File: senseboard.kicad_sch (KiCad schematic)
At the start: 81 parts, among them J1 USB_C_Receptacle_USB2.0_16P, J2 Screw_Terminal_01x02, J3 DM3AT-SF-PEJM5, J4 Conn_01x04, J5 Conn_01x08, U1 USBLC6-2SC6, U10 EMIF06-MSD02N16, U11 BME690, U2 TPS62840DLCR, U3 TPS62840DLCR, U4 SCD41-D-R2, U5 SGP41-D-R4, U6 SGP41-D-R4, U7 SHT4x, U8 STM32L4Q5CGUx, U9 RFM95W-915S2, Y1 Crystal_GND3

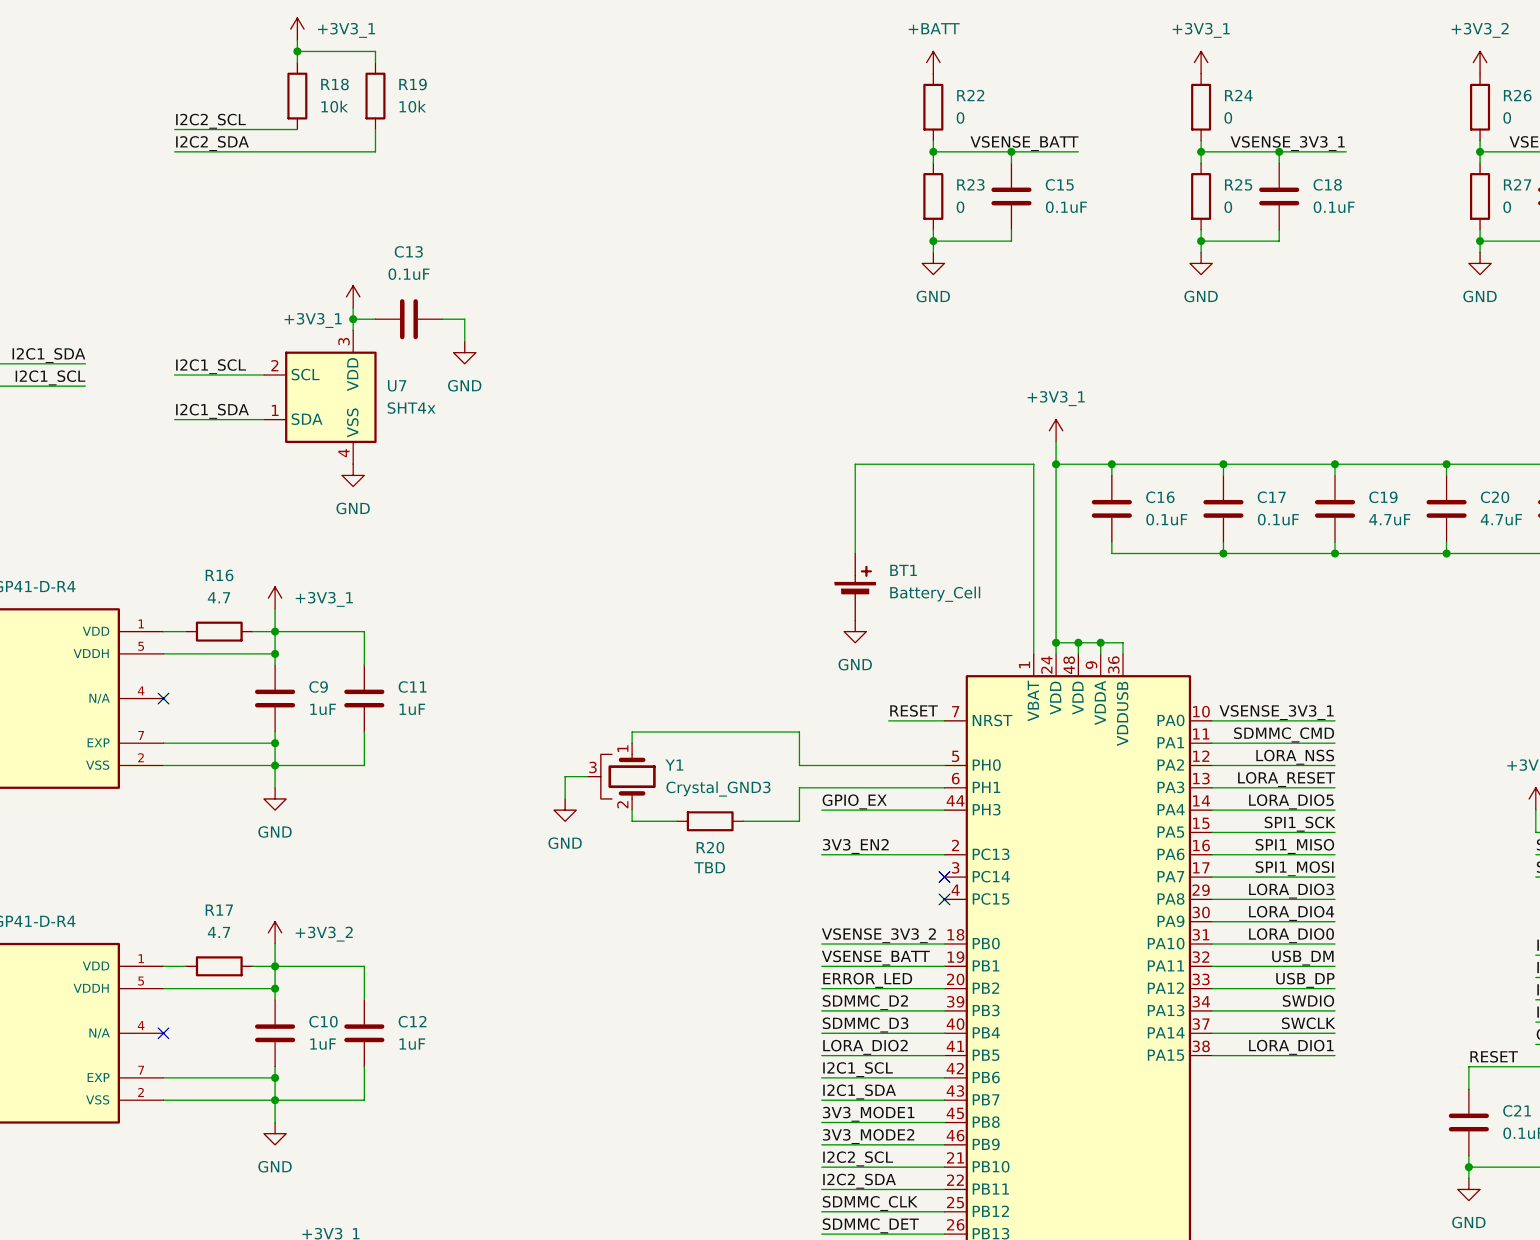
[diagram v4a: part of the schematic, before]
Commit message: connected n/a on sgp41 to gnd
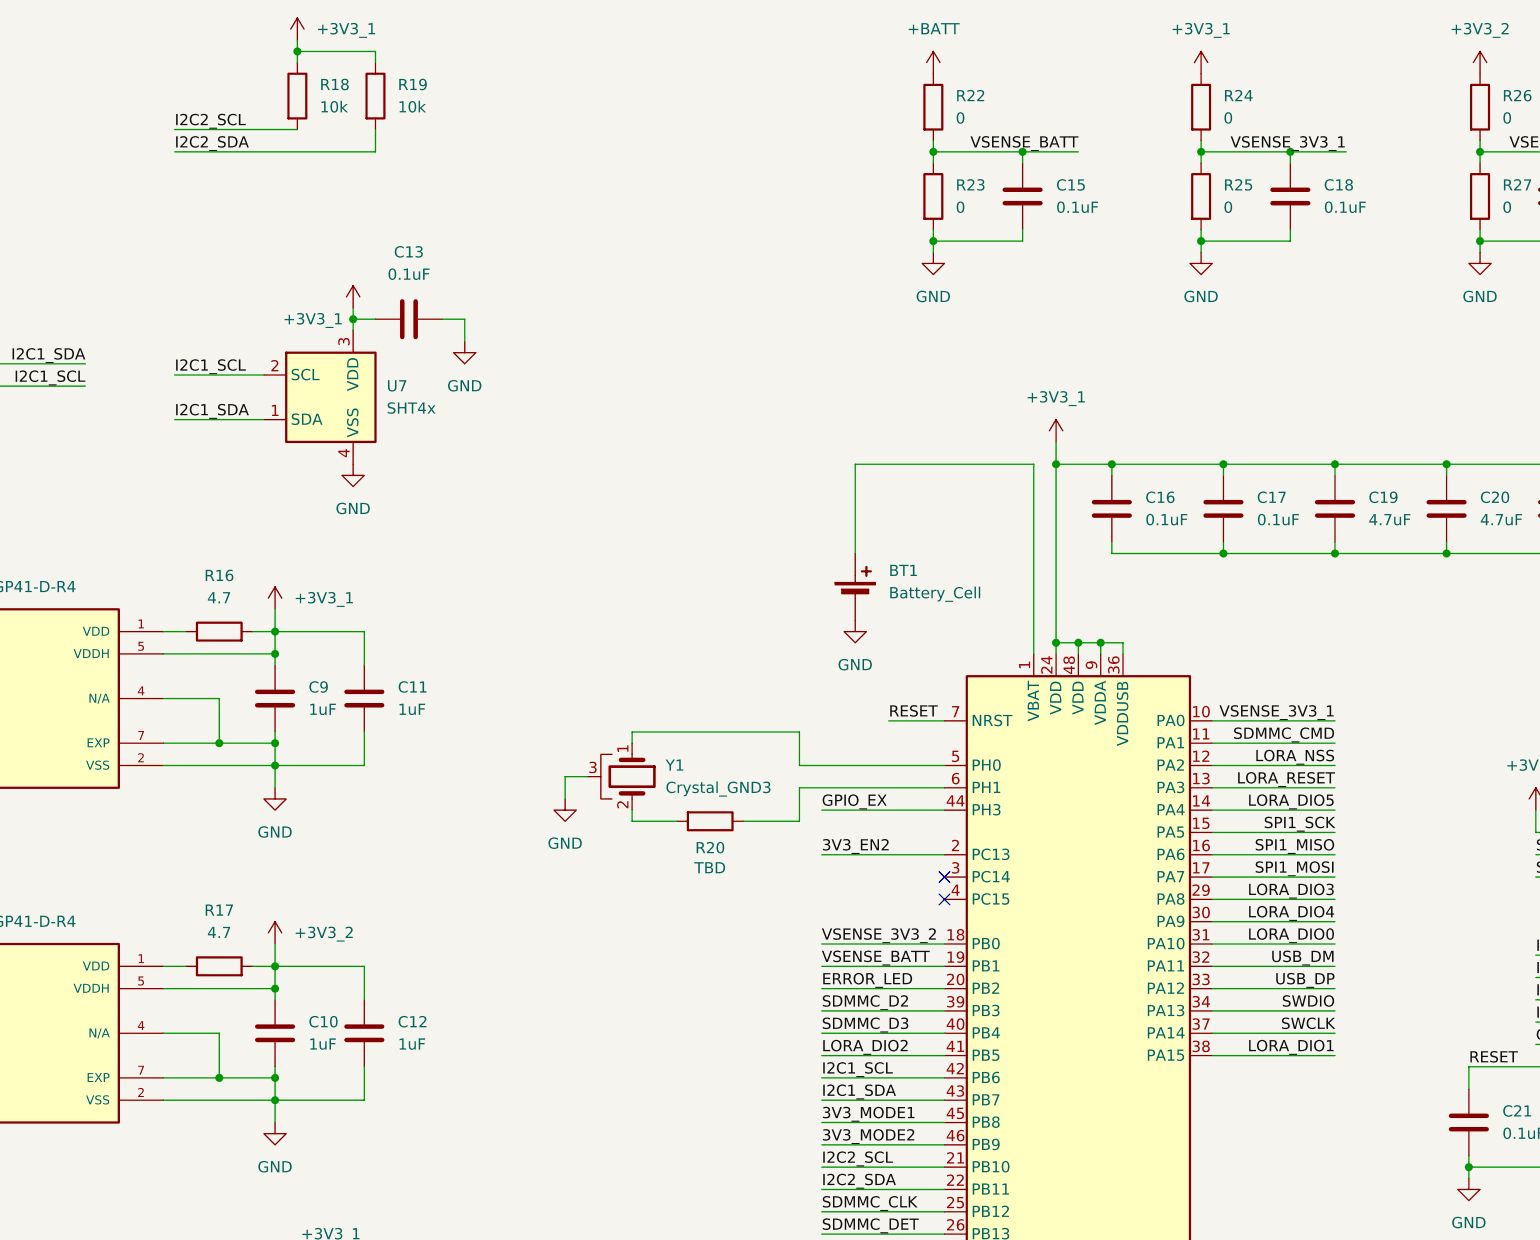
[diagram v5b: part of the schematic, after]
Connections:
- net GND: now also U5.4 (N/A), U6.4 (N/A)
- no-connect marks 9 -> 7
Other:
- moved on the sheet: C15, C18
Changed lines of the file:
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@@
 	)
 	(junction
-		(at 320.04 39.37)
-		(diameter 0)
-		(color 0 0 0 0)
-	)
-	(junction
 		(at 243.84 241.3)
 		(diameter 0)
@@
 	)
 	(junction
+		(at 229.87 106.68)
+		(diameter 0)
+		(color 0 0 0 0)
+	)
+	(junction
 		(at 344.17 74.93)
 		(diameter 0)
@@
 	)
 	(junction
+		(at 351.79 39.37)
+		(diameter 0)
+		(color 0 0 0 0)
+	)
+	(junction
 		(at 373.38 49.53)
 		(diameter 0)
@@
 	)
 	(junction
+		(at 321.31 39.37)
+		(diameter 0)
+		(color 0 0 0 0)
+	)
+	(junction
 		(at 67.31 208.28)
 		(diameter 0)
@@
 	)
 	(junction
+		(at 229.87 144.78)
+		(diameter 0)
+		(color 0 0 0 0)
+	)
+	(junction
 		(at 311.15 39.37)
 		(diameter 0)
@@
 	)
 	(junction
-		(at 350.52 39.37)
-		(diameter 0)
-		(color 0 0 0 0)
-	)
-	(junction
 		(at 78.74 190.5)
 		(diameter 0)
@@
 	)
 	(no_connect
-		(at 223.52 101.6)
-	)
-	(no_connect
-		(at 223.52 139.7)
-	)
-	(no_connect
 		(at 85.09 149.86)
 	)
@@
 	(wire
 		(pts
+			(xy 229.87 144.78) (xy 236.22 144.78)
+		)
+		(stroke
+			(width 0)
+			(type default)
+		)
+	)
+	(wire
+		(pts
 			(xy 222.25 226.06) (xy 214.63 226.06)
 		)
@@
 	(wire
 		(pts
-			(xy 320.04 40.64) (xy 320.04 39.37)
+			(xy 321.31 40.64) (xy 321.31 39.37)
 		)
 		(stroke
@@
 	(wire
 		(pts
-			(xy 350.52 40.64) (xy 350.52 39.37)
+			(xy 351.79 40.64) (xy 351.79 39.37)
 		)
 		(stroke
@@
 	(wire
 		(pts
-			(xy 350.52 39.37) (xy 358.14 39.37)
-		)
-		(stroke
-			(width 0)
-			(type default)
-		)
-	)
-	(wire
-		(pts
 			(xy 228.6 173.99) (xy 227.33 173.99)
 		)
@@
 	(wire
 		(pts
-			(xy 223.52 106.68) (xy 236.22 106.68)
+			(xy 223.52 106.68) (xy 229.87 106.68)
 		)
 		(stroke
@@
 	(wire
 		(pts
+			(xy 321.31 39.37) (xy 327.66 39.37)
+		)
+		(stroke
+			(width 0)
+			(type default)
+		)
+	)
+	(wire
+		(pts
 			(xy 120.65 133.35) (xy 123.19 133.35)
 		)
@@
 	(wire
 		(pts
+			(xy 229.87 106.68) (xy 236.22 106.68)
+		)
+		(stroke
+			(width 0)
+			(type default)
+		)
+	)
+	(wire
+		(pts
 			(xy 60.96 210.82) (xy 67.31 210.82)
 		)
@@
 	(wire
 		(pts
+			(xy 351.79 39.37) (xy 358.14 39.37)
+		)
+		(stroke
+			(width 0)
+			(type default)
+		)
+	)
+	(wire
+		(pts
 			(xy 372.11 215.9) (xy 374.65 215.9)
 		)
@@
 	(wire
 		(pts
-			(xy 341.63 49.53) (xy 350.52 49.53)
+			(xy 341.63 49.53) (xy 351.79 49.53)
 		)
 		(stroke
@@
 	(wire
 		(pts
+			(xy 229.87 139.7) (xy 229.87 144.78)
+		)
+		(stroke
+			(width 0)
+			(type default)
+		)
+	)
+	(wire
+		(pts
 			(xy 196.85 39.37) (xy 196.85 36.83)
 		)
@@
 	(wire
 		(pts
-			(xy 350.52 49.53) (xy 350.52 48.26)
+			(xy 351.79 49.53) (xy 351.79 48.26)
 		)
 		(stroke
@@
 	(wire
 		(pts
-			(xy 320.04 49.53) (xy 320.04 48.26)
+			(xy 321.31 49.53) (xy 321.31 48.26)
 		)
 		(stroke
@@
 	(wire
 		(pts
-			(xy 320.04 39.37) (xy 327.66 39.37)
-		)
-		(stroke
-			(width 0)
-			(type default)
-		)
-	)
-	(wire
-		(pts
 			(xy 344.17 76.2) (xy 344.17 74.93)
 		)
@@
 	(wire
 		(pts
-			(xy 223.52 144.78) (xy 236.22 144.78)
+			(xy 223.52 144.78) (xy 229.87 144.78)
 		)
 		(stroke
@@
 	(wire
 		(pts
-			(xy 311.15 49.53) (xy 320.04 49.53)
+			(xy 311.15 49.53) (xy 321.31 49.53)
 		)
 		(stroke
@@
 	(wire
 		(pts
+			(xy 229.87 101.6) (xy 229.87 106.68)
+		)
+		(stroke
+			(width 0)
+			(type default)
+		)
+	)
+	(wire
+		(pts
 			(xy 236.22 96.52) (xy 236.22 93.98)
 		)
@@
 	(wire
 		(pts
+			(xy 223.52 101.6) (xy 229.87 101.6)
+		)
+		(stroke
+			(width 0)
+			(type default)
+		)
+	)
+	(wire
+		(pts
 			(xy 342.9 137.16) (xy 356.87 137.16)
 		)
@@
 	(wire
 		(pts
-			(xy 311.15 39.37) (xy 320.04 39.37)
+			(xy 311.15 39.37) (xy 321.31 39.37)
 		)
 		(stroke
@@
 	(wire
 		(pts
+			(xy 223.52 139.7) (xy 229.87 139.7)
+		)
+		(stroke
+			(width 0)
+			(type default)
+		)
+	)
+	(wire
+		(pts
 			(xy 247.65 39.37) (xy 247.65 36.83)
 		)
@@
 	(wire
 		(pts
-			(xy 341.63 39.37) (xy 350.52 39.37)
+			(xy 341.63 39.37) (xy 351.79 39.37)
 		)
 		(stroke
@@
 	(symbol
 		(lib_id "Device:C")
-		(at 350.52 44.45 0)
+		(at 351.79 44.45 0)
 		(unit 1)
 		(body_style 1)
@@
 		(fields_autoplaced yes)
 		(property "Reference" "C18"
-			(at 354.33 43.1799 0)
+			(at 355.6 43.1799 0)
 			(show_name no)
 			(do_not_autoplace no)
@@
 		)
 		(property "Value" "0.1uF"
-			(at 354.33 45.7199 0)
+			(at 355.6 45.7199 0)
 			(show_name no)
 			(do_not_autoplace no)
@@
 		)
 		(property "Footprint" "Capacitor_SMD:C_0402_1005Metric"
-			(at 351.4852 48.26 0)
+			(at 352.7552 48.26 0)
 			(hide yes)
 			(show_name no)
@@
 		)
 		(property "Datasheet" ""
-			(at 350.52 44.45 0)
+			(at 351.79 44.45 0)
 			(hide yes)
 			(show_name no)
@@
 		)
 		(property "Description" "Unpolarized capacitor"
-			(at 350.52 44.45 0)
+			(at 351.79 44.45 0)
 			(hide yes)
 			(show_name no)
@@
 					(reference "R25")
 					(unit 1)
+					(variant
+						(name "STD")
+						(field
+							(name "Value")
+							(value "50k")
+						)
+					)
 				)
 			)
@@
 					(reference "R22")
 					(unit 1)
+					(variant
+						(name "STD")
+						(field
+							(name "Value")
+							(value "50k")
+						)
+					)
 				)
 			)
@@
 					(reference "R24")
 					(unit 1)
+					(variant
+						(name "STD")
+						(field
+							(name "Value")
+							(value "50k")
+						)
+					)
 				)
 			)
@@
 					(reference "R26")
 					(unit 1)
+					(variant
+						(name "STD")
+						(field
+							(name "Value")
+							(value "50k")
+						)
+					)
 				)
 			)
@@
 					(reference "R23")
 					(unit 1)
+					(variant
+						(name "STD")
+						(field
+							(name "Value")
+							(value "50k")
+						)
+					)
 				)
 			)
@@
 					(reference "R29")
 					(unit 1)
+					(variant
+						(name "STD")
+						(dnp yes)
+					)
 				)
 			)
@@
 					(reference "R27")
 					(unit 1)
+					(variant
+						(name "STD")
+						(field
+							(name "Value")
+							(value "50k")
+						)
+					)
 				)
 			)
@@
 	(symbol
 		(lib_id "Device:C")
-		(at 320.04 44.45 0)
+		(at 321.31 44.45 0)
 		(unit 1)
 		(body_style 1)
@@
 		(fields_autoplaced yes)
 		(property "Reference" "C15"
-			(at 323.85 43.1799 0)
+			(at 325.12 43.1799 0)
 			(show_name no)
 			(do_not_autoplace no)
@@
 		)
 		(property "Value" "0.1uF"
-			(at 323.85 45.7199 0)
+			(at 325.12 45.7199 0)
 			(show_name no)
 			(do_not_autoplace no)
@@
 		)
 		(property "Footprint" "Capacitor_SMD:C_0402_1005Metric"
-			(at 321.0052 48.26 0)
+			(at 322.2752 48.26 0)
 			(hide yes)
 			(show_name no)
@@
 		)
 		(property "Datasheet" ""
-			(at 320.04 44.45 0)
+			(at 321.31 44.45 0)
 			(hide yes)
 			(show_name no)
@@
 		)
 		(property "Description" "Unpolarized capacitor"
-			(at 320.04 44.45 0)
+			(at 321.31 44.45 0)
 			(hide yes)
 			(show_name no)

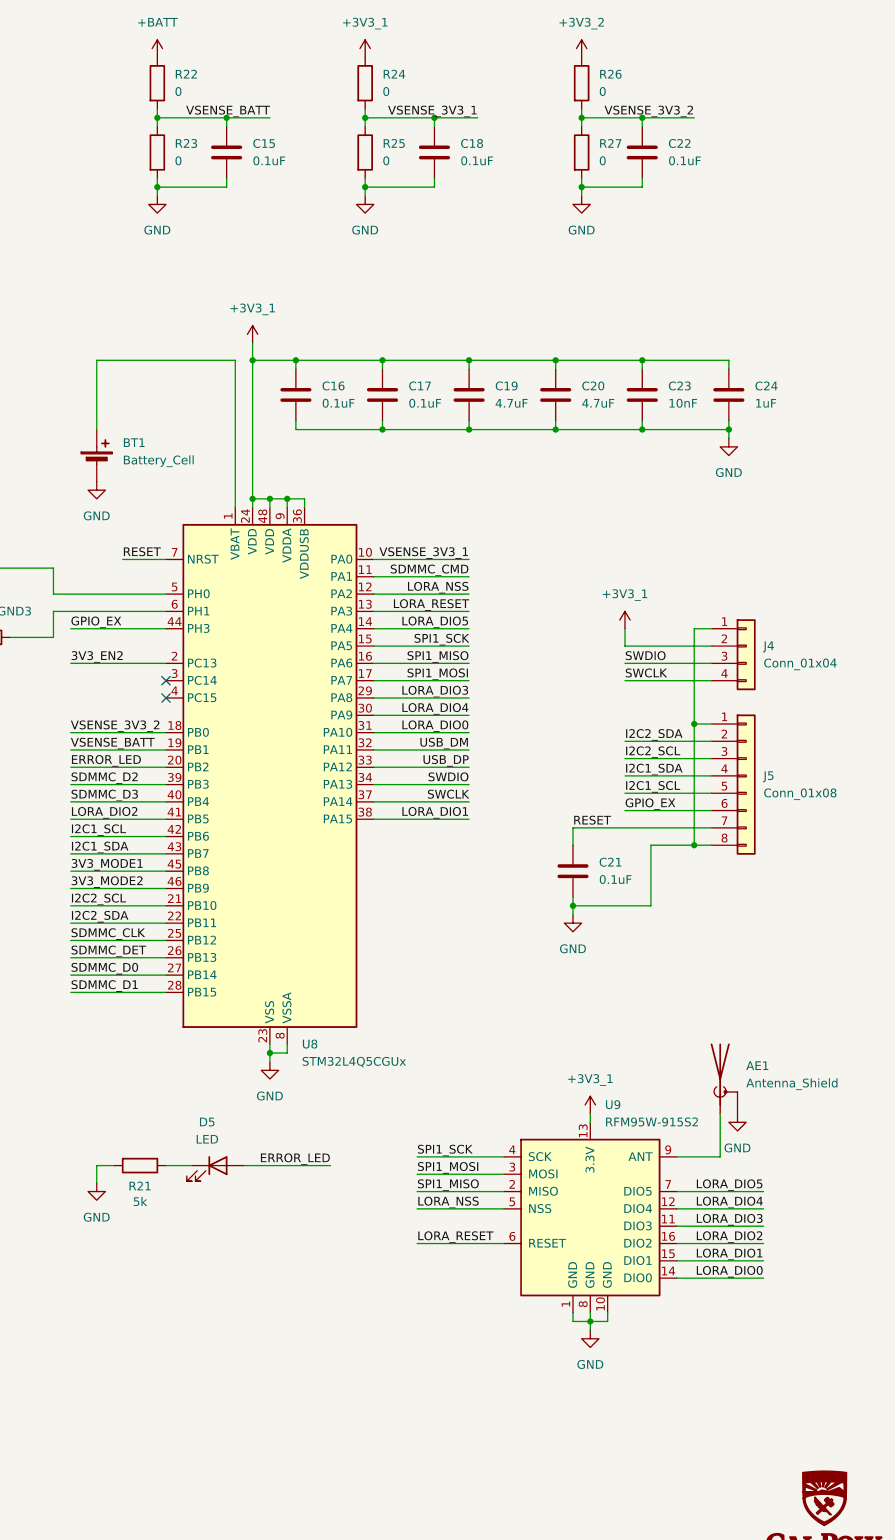
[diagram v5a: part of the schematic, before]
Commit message: added values and variant for assembly, added 3d model for sd protection to layout, played with via setup
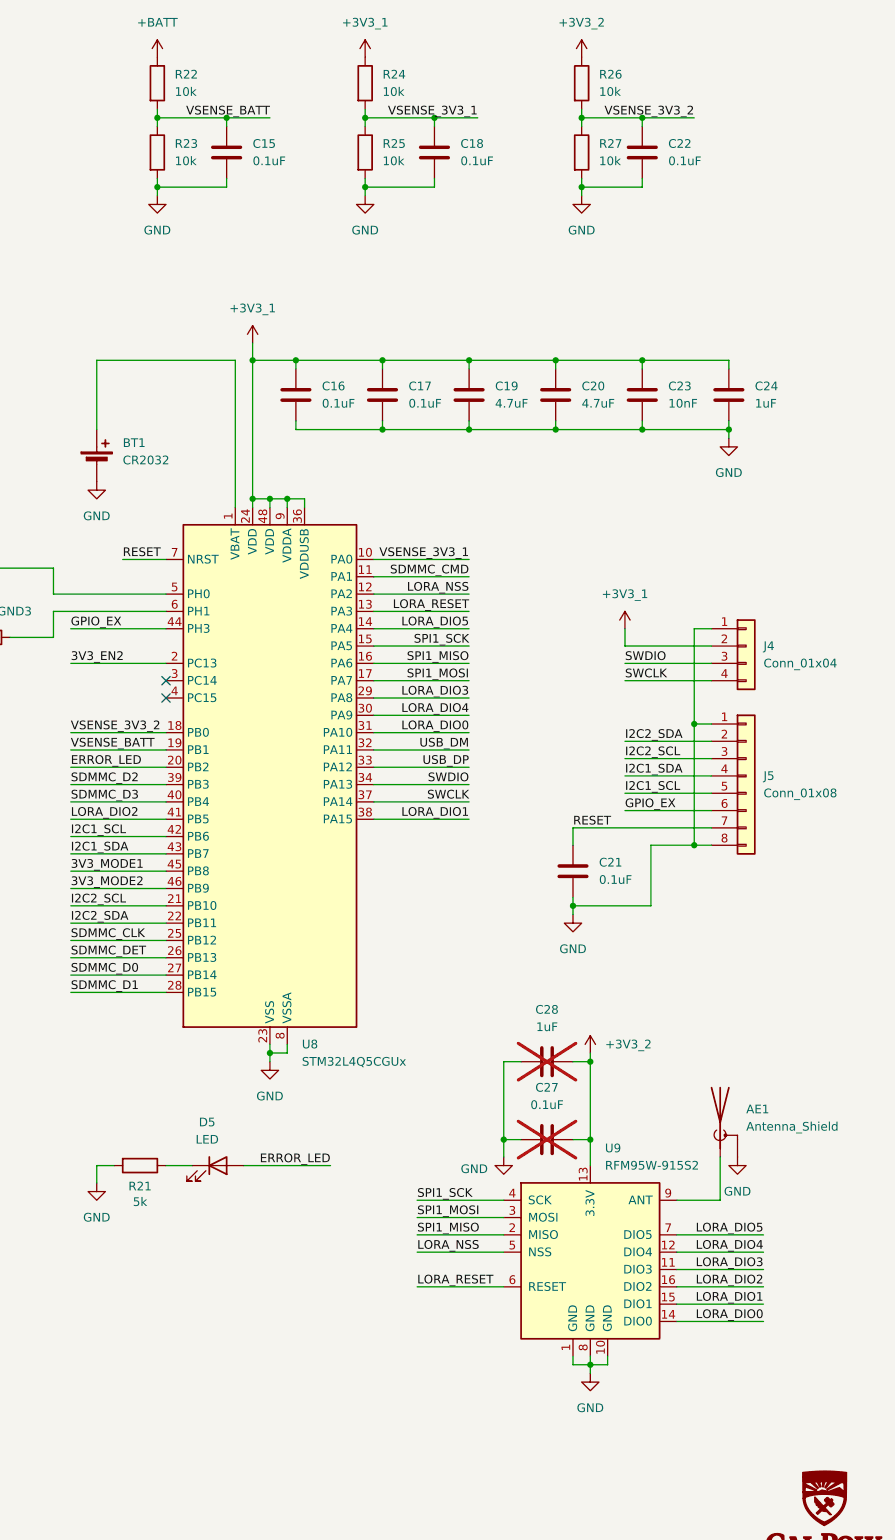
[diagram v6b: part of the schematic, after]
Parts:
- added C27: 0.1uF, Capacitor_SMD:C_0603_1608Metric, symbol Device:C
- added C28: 1uF, Capacitor_SMD:C_0805_2012Metric, symbol Device:C
- BT1: value Battery_Cell -> CR2032
- R22, R23, R24, R25, R26, R27: value 0 -> 10k
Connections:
- net +3V3_1: no longer U9.13 (3.3V)
- net +3V3_2: now also U9.13 (3.3V), C27.1, C28.1
- net GND: now also C27.2, C28.2
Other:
- moved on the sheet: AE1, U9
